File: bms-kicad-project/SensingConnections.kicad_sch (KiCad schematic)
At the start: 29 parts, among them J10 XT60PW-F, J11 1053131302, J12 XT60PW-F, J13 1053131302, J14 1053131303, J15 XT60PW-F, J16 SM06B-GHS-TB, J17 5024940670, J6 XT60PW-F, J7 1053131302, J8 XT60PW-M, J9 1053131302, U8 ACS72981KLRATR-150B5

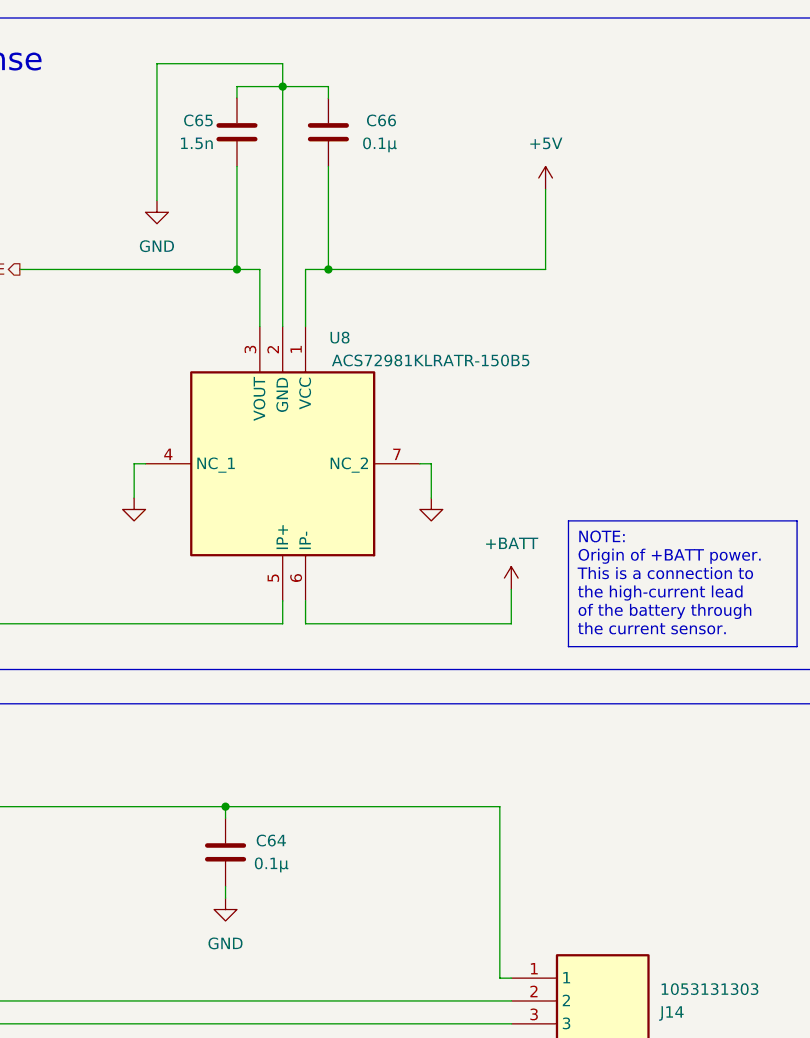
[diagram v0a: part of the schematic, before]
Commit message: feat: added sims directory, new cell balancing components
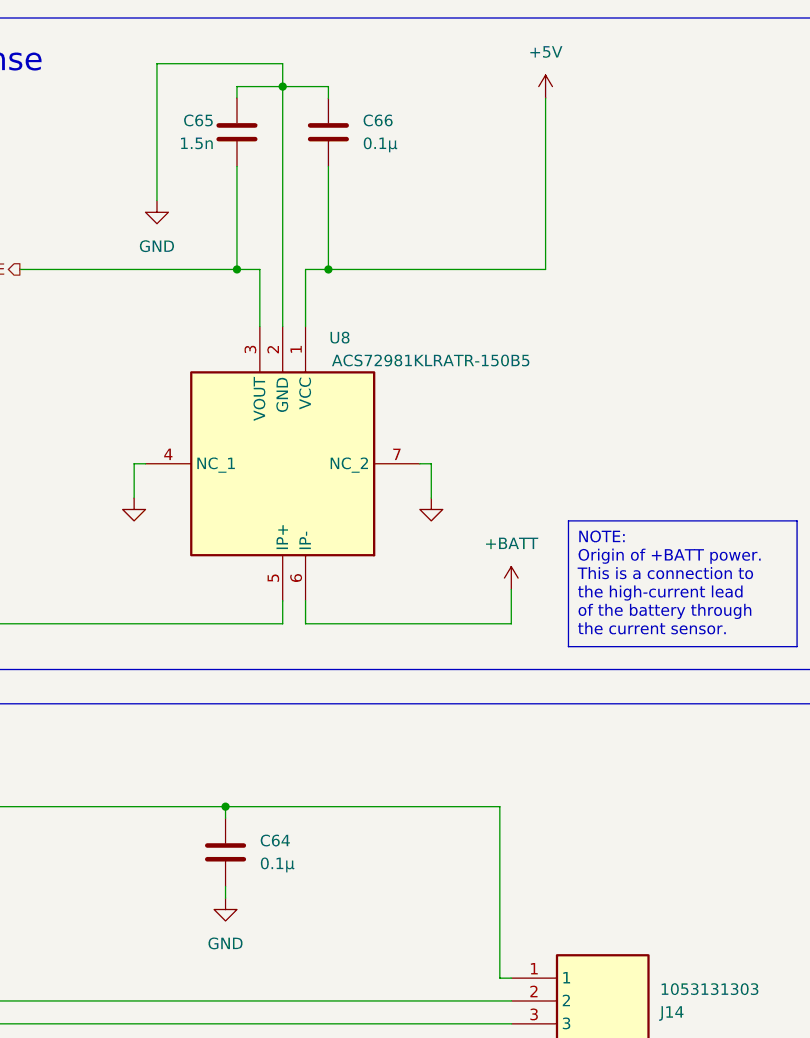
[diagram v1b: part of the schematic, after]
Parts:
- removed C64, C66: 0.1µ, FixedWing:G-21_MUR, symbol FixedWing:GCM21BR72A104KA37L
- added C64, C66: 0.1µ, FixedWing:CAP_GCJ-18_MUR, symbol FixedWing:GCJ188R72A104KA01D
- J10, J12, J15, J6: Manufacturer (none) -> Amass
- J8: Manufacturer (none) -> Changzou Amass Elec
- R109, R110: Manufacturer (none) -> Vishay; Manufacturer Part Number (none) -> CRCW0805100RFKEA
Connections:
- net +5V: now also C64.2, C66.1
- net GND: now also C64.1, C66.2
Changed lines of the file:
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@@
     (stroke (width 0) (type default))
   )
-  (wire (pts (xy 124.46 34.29) (xy 124.46 43.18))
+  (wire (pts (xy 124.46 24.13) (xy 124.46 43.18))
     (stroke (width 0) (type default))
   )
@@
       (effects (font (size 1.27 1.27)) (justify left top) hide)
     )
+    (property "Manufacturer" "Vishay" (at 104.14 884.15 0)
+      (effects (font (size 1.27 1.27)) (justify left top) hide)
+    )
+    (property "Manufacturer Part Number" "CRCW0805100RFKEA" (at 104.14 984.15 0)
+      (effects (font (size 1.27 1.27)) (justify left top) hide)
+    )
     (pin "2")
     (pin "1")
@@
     )
     (property "Arrow Price/Stock" "" (at 26.67 -945.39 0)
+      (effects (font (size 1.27 1.27)) (justify left top) hide)
+    )
+    (property "Manufacturer" "Changzou Amass Elec" (at 26.67 -445.39 0)
       (effects (font (size 1.27 1.27)) (justify left top) hide)
     )
@@
     )
   )
-  (symbol (lib_id "FixedWing:GCM21BR72A104KA37L") (at 100.33 24.13 90) (mirror x) (unit 1)
-    (in_bom yes) (on_board yes) (dnp no)
-    (property "Reference" "C66" (at 107.95 26.67 90)
-      (effects (font (size 1.27 1.27)) (justify left))
-    )
-    (property "Value" "0.1µ" (at 107.95 29.21 90)
-      (effects (font (size 1.27 1.27)) (justify left))
-    )
-    (property "Footprint" "FixedWing:G-21_MUR" (at 86.36 24.13 0)
-      (effects (font (size 1.27 1.27) italic) hide)
-    )
-    (property "Datasheet" "https://search.murata.co.jp/Ceramy/image/img/A01X/G101/ENG/GCJ21BR71A106KE01-01A.pdf" (at 88.9 24.13 0)
-      (effects (font (size 1.27 1.27) italic) hide)
-    )
-    (property "Manufacturer" "Murata Electronics" (at 91.44 24.13 0)
-      (effects (font (size 1.27 1.27)) hide)
-    )
-    (property "Manufacturer Part Number" "GCM21BR72A104KA37L" (at 93.98 24.13 0)
-      (effects (font (size 1.27 1.27)) hide)
-    )
-    (pin "1")
-    (pin "2")
-    (instances
-      (project "bms-board"
-        (path "/8a7831d1-a913-4f04-8780-225d2234b41d/9cf0d325-c2d4-4535-a4db-163de33edbd1"
-          (reference "C66") (unit 1)
-        )
-      )
-    )
-  )
   (symbol (lib_id "FixedWing:XT60PW-F") (at 234.95 46.99 0) (unit 1)
     (in_bom yes) (on_board yes) (dnp no)
@@
     )
     (property "Arrow Price/Stock" "" (at 254 1041.91 0)
+      (effects (font (size 1.27 1.27)) (justify left top) hide)
+    )
+    (property "Manufacturer" "Amass" (at 254 541.91 0)
       (effects (font (size 1.27 1.27)) (justify left top) hide)
     )
@@
     )
   )
+  (symbol (lib_id "FixedWing:GCJ188R72A104KA01D") (at 88.9 111.76 90) (unit 1)
+    (in_bom yes) (on_board yes) (dnp no) (fields_autoplaced)
+    (property "Reference" "C64" (at 92.71 106.68 90)
+      (effects (font (size 1.27 1.27)) (justify right))
+    )
+    (property "Value" "0.1µ" (at 92.71 109.22 90)
+      (effects (font (size 1.27 1.27)) (justify right))
+    )
+    (property "Footprint" "FixedWing:CAP_GCJ-18_MUR" (at 77.47 114.3 0)
+      (effects (font (size 1.27 1.27) italic) hide)
+    )
+    (property "Datasheet" "https://search.murata.co.jp/Ceramy/image/img/A01X/G101/ENG/GCJ21BR71A106KE01-01A.pdf" (at 77.47 114.3 0)
+      (effects (font (size 1.27 1.27) italic) hide)
+    )
+    (property "Manufacturer" "Murata Electronics" (at 77.47 113.03 0)
+      (effects (font (size 1.27 1.27)) hide)
+    )
+    (property "Manufacturer Part Number" "GCJ188R72A104KA01D" (at 77.47 114.3 0)
+      (effects (font (size 1.27 1.27)) hide)
+    )
+    (pin "2")
+    (pin "1")
+    (instances
+      (project "bms-board"
+        (path "/8a7831d1-a913-4f04-8780-225d2234b41d/9cf0d325-c2d4-4535-a4db-163de33edbd1"
+          (reference "C64") (unit 1)
+        )
+      )
+    )
+  )
   (symbol (lib_id "Mechanical:MountingHole_Pad") (at 406.4 217.17 90) (mirror x) (unit 1)
     (in_bom yes) (on_board yes) (dnp no) (fields_autoplaced)
@@
     )
     (property "Arrow Price/Stock" "" (at 288.29 1041.91 0)
+      (effects (font (size 1.27 1.27)) (justify left top) hide)
+    )
+    (property "Manufacturer" "Amass" (at 288.29 541.91 0)
       (effects (font (size 1.27 1.27)) (justify left top) hide)
     )
@@
     )
   )
-  (symbol (lib_id "power:+5V") (at 124.46 34.29 0) (unit 1)
-    (in_bom yes) (on_board yes) (dnp no) (fields_autoplaced)
-    (property "Reference" "#PWR067" (at 124.46 38.1 0)
-      (effects (font (size 1.27 1.27)) hide)
-    )
-    (property "Value" "+5V" (at 124.46 29.21 0)
-      (effects (font (size 1.27 1.27)))
-    )
-    (property "Footprint" "" (at 124.46 34.29 0)
-      (effects (font (size 1.27 1.27)) hide)
-    )
-    (property "Datasheet" "" (at 124.46 34.29 0)
+  (symbol (lib_id "power:+5V") (at 124.46 24.13 0) (unit 1)
+    (in_bom yes) (on_board yes) (dnp no) (fields_autoplaced)
+    (property "Reference" "#PWR067" (at 124.46 27.94 0)
+      (effects (font (size 1.27 1.27)) hide)
+    )
+    (property "Value" "+5V" (at 124.46 19.05 0)
+      (effects (font (size 1.27 1.27)))
+    )
+    (property "Footprint" "" (at 124.46 24.13 0)
+      (effects (font (size 1.27 1.27)) hide)
+    )
+    (property "Datasheet" "" (at 124.46 24.13 0)
       (effects (font (size 1.27 1.27)) hide)
     )
@@
     )
   )
-  (symbol (lib_id "FixedWing:GCM21BR72A104KA37L") (at 88.9 111.76 90) (unit 1)
-    (in_bom yes) (on_board yes) (dnp no)
-    (property "Reference" "C64" (at 93.98 106.68 90)
-      (effects (font (size 1.27 1.27)))
-    )
-    (property "Value" "0.1µ" (at 93.98 109.22 90)
-      (effects (font (size 1.27 1.27)))
-    )
-    (property "Footprint" "FixedWing:G-21_MUR" (at 74.93 111.76 0)
-      (effects (font (size 1.27 1.27) italic) hide)
-    )
-    (property "Datasheet" "https://search.murata.co.jp/Ceramy/image/img/A01X/G101/ENG/GCJ21BR71A106KE01-01A.pdf" (at 77.47 111.76 0)
-      (effects (font (size 1.27 1.27) italic) hide)
-    )
-    (property "Manufacturer" "Murata Electronics" (at 80.01 111.76 0)
-      (effects (font (size 1.27 1.27)) hide)
-    )
-    (property "Manufacturer Part Number" "GCM21BR72A104KA37L" (at 82.55 111.76 0)
-      (effects (font (size 1.27 1.27)) hide)
-    )
-    (pin "1")
-    (pin "2")
-    (instances
-      (project "bms-board"
-        (path "/8a7831d1-a913-4f04-8780-225d2234b41d/9cf0d325-c2d4-4535-a4db-163de33edbd1"
-          (reference "C64") (unit 1)
-        )
-      )
-    )
-  )
   (symbol (lib_id "FixedWing:XT60PW-F") (at 200.66 46.99 0) (unit 1)
     (in_bom yes) (on_board yes) (dnp no)
@@
     )
     (property "Arrow Price/Stock" "" (at 219.71 1041.91 0)
+      (effects (font (size 1.27 1.27)) (justify left top) hide)
+    )
+    (property "Manufacturer" "Amass" (at 219.71 541.91 0)
       (effects (font (size 1.27 1.27)) (justify left top) hide)
     )
@@
       (effects (font (size 1.27 1.27)) (justify left top) hide)
     )
+    (property "Manufacturer" "Vishay" (at 113.03 884.15 0)
+      (effects (font (size 1.27 1.27)) (justify left top) hide)
+    )
+    (property "Manufacturer Part Number" "CRCW0805100RFKEA" (at 113.03 984.15 0)
+      (effects (font (size 1.27 1.27)) (justify left top) hide)
+    )
     (pin "1")
     (pin "2")
@@
     )
   )
+  (symbol (lib_id "FixedWing:GCJ188R72A104KA01D") (at 100.33 31.75 90) (unit 1)
+    (in_bom yes) (on_board yes) (dnp no) (fields_autoplaced)
+    (property "Reference" "C66" (at 104.14 26.67 90)
+      (effects (font (size 1.27 1.27)) (justify right))
+    )
+    (property "Value" "0.1µ" (at 104.14 29.21 90)
+      (effects (font (size 1.27 1.27)) (justify right))
+    )
+    (property "Footprint" "FixedWing:CAP_GCJ-18_MUR" (at 88.9 34.29 0)
+      (effects (font (size 1.27 1.27) italic) hide)
+    )
+    (property "Datasheet" "https://search.murata.co.jp/Ceramy/image/img/A01X/G101/ENG/GCJ21BR71A106KE01-01A.pdf" (at 88.9 34.29 0)
+      (effects (font (size 1.27 1.27) italic) hide)
+    )
+    (property "Manufacturer" "Murata Electronics" (at 88.9 33.02 0)
+      (effects (font (size 1.27 1.27)) hide)
+    )
+    (property "Manufacturer Part Number" "GCJ188R72A104KA01D" (at 88.9 34.29 0)
+      (effects (font (size 1.27 1.27)) hide)
+    )
+    (pin "1")
+    (pin "2")
+    (instances
+      (project "bms-board"
+        (path "/8a7831d1-a913-4f04-8780-225d2234b41d/9cf0d325-c2d4-4535-a4db-163de33edbd1"
+          (reference "C66") (unit 1)
+        )
+      )
+    )
+  )
   (symbol (lib_id "power:+BATT") (at 165.1 30.48 0) (unit 1)
     (in_bom yes) (on_board yes) (dnp no) (fields_autoplaced)
@@
       (effects (font (size 1.27 1.27)) (justify left top) hide)
     )
+    (property "Manufacturer" "Amass" (at 185.42 541.91 0)
+      (effects (font (size 1.27 1.27)) (justify left top) hide)
+    )

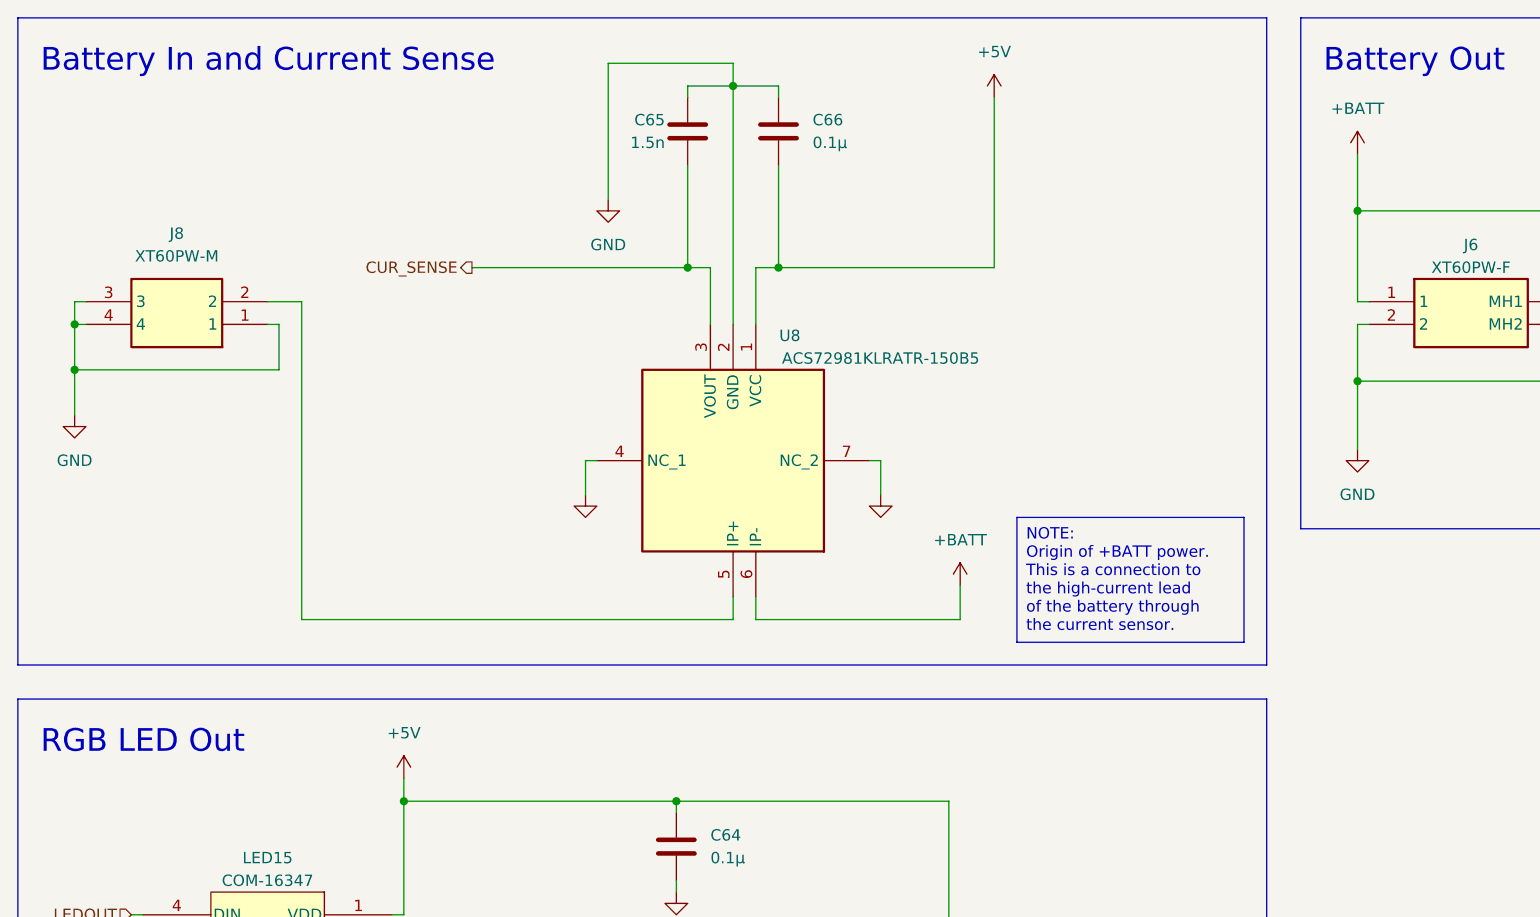
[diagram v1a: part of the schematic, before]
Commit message: feat: cell filtering/balancing switchover done
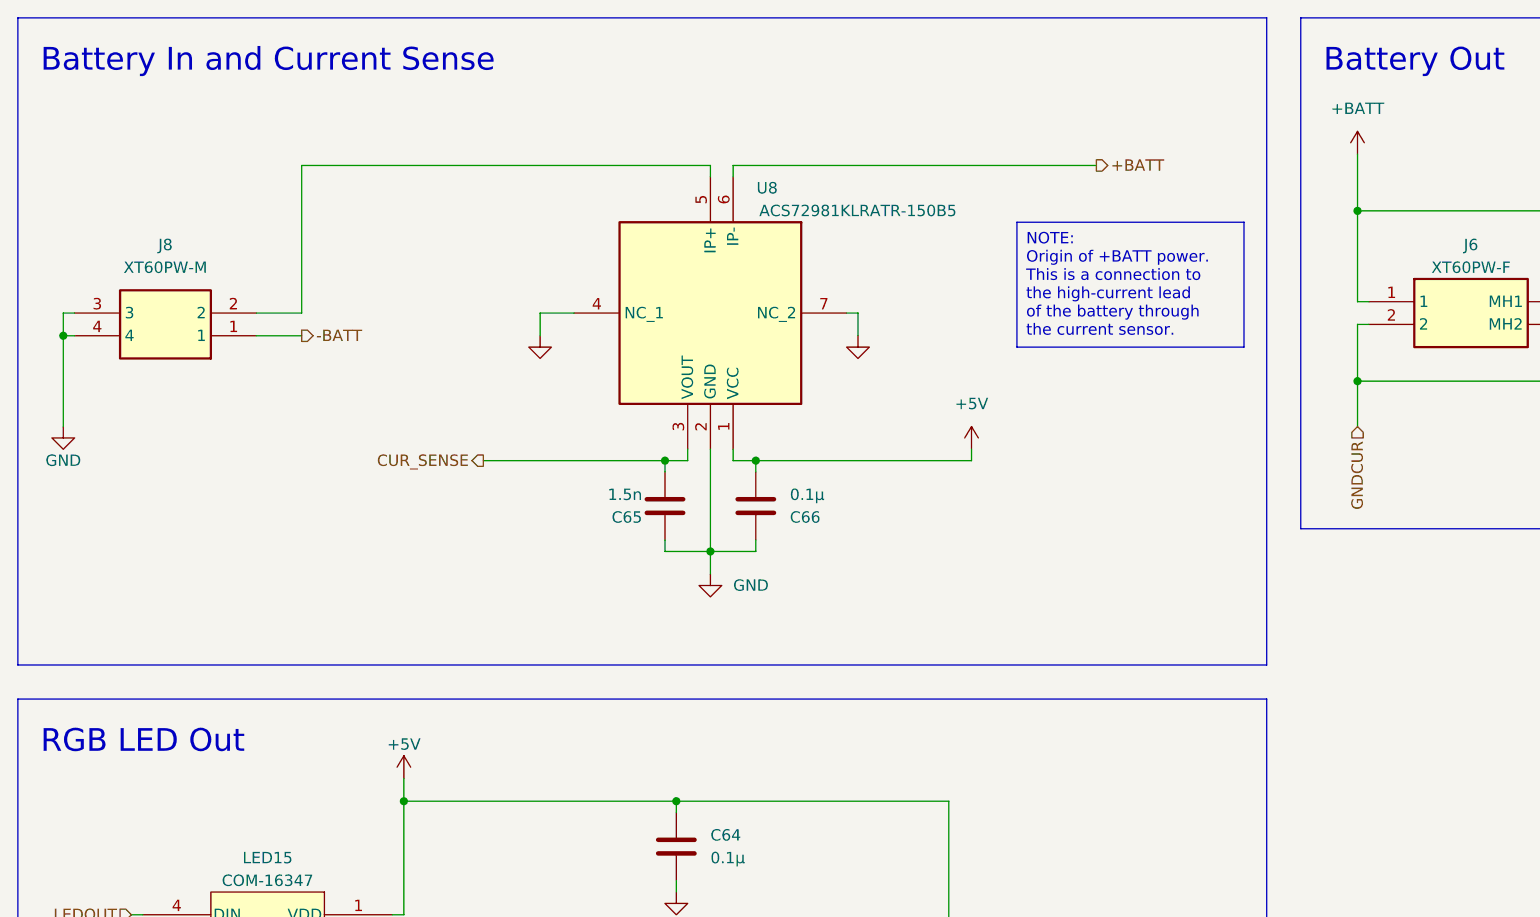
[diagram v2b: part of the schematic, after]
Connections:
- net GND: no longer J10.2, J10.3 (MH1), J10.4 (MH2), J12.2, J12.3 (MH1), J12.4 (MH2), J15.2, J15.3 (MH1), J15.4 (MH2), J6.2, J6.3 (MH1), J6.4 (MH2), J8.1
- new net -BATT: J8.1
- new net GNDCUR: J10.2, J10.3 (MH1), J10.4 (MH2), J12.2, J12.3 (MH1), J12.4 (MH2), J15.2, J15.3 (MH1), J15.4 (MH2), J6.2, J6.3 (MH1), J6.4 (MH2)
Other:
- moved on the sheet: C65, C66, J8, U8

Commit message: feat: don't even know what I changed, just zoned out for several hours. Made PCB r/a mount XT-60s and solder pads into a 2-for-1 deal
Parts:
- added J18: XT60PW-F, FixedWing:XT60PWF, symbol FixedWing:XT60PW-F
- J13: renamed from J15; footprint FixedWing:XT60PWF -> FixedWing:XT60PWF_Pad
- J6: renamed from J8; footprint FixedWing:XT60PWM -> FixedWing:XT60PWM_Pad
- renumbered C64 to C66, C66 to C67, J6 to J10, J10 to J11, J7 to J14, J9 to J15, J11 to J16, J13 to J17, J17 to J7, J14 to J8, J16 to J9, R108 to R120, R109 to R121, R110 to R122, R111 to R123, U8 to U7
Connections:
- net +BATT: now also J18.1
- net GND: now also J10.3 (MH1), J10.4 (MH2), J11.3 (MH1), J11.4 (MH2), J12.3 (MH1), J12.4 (MH2), J9.7, J9.8, J18.3 (MH1), J18.4 (MH2); no longer J6.3, J6.4
- net GNDCUR: now also J18.2; no longer J10.3 (MH1), J10.4 (MH2), J11.3 (MH1), J11.4 (MH2), J12.3 (MH1), J12.4 (MH2), J13.3 (MH1), J13.4 (MH2)
- net RGB_DOUT: now reaches J8.2, LED15.2 (DOUT)
- net LEDOUT renamed RGB_DIN
- no-connect marks 0 -> 4
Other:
- moved on the sheet: C66, J11, J12, J13, J14, J15, J16, J17, J7, J8, LED15, R120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

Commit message: feat: schematic pretty much done
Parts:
- added TP19, TP20, TP21: TestPoint, TestPoint:TestPoint_Pad_D1.5mm, symbol Connector:TestPoint
- renumbered C66 to C65, C65 to C66, J12 to J10, J18 to J11, J8 to J12, J9 to J13, J13 to J14, J14 to J15, J15 to J16, J16 to J17, J17 to J18, J10 to J6, J6 to J7, J11 to J8, J7 to J9
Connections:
- net +BATT: now also TP21.1
- net CUR_SENSE: now also TP19.1
- net GND: no longer J15.2, J16.2, J17.2, J18.2
- net GNDCUR: now also J15.2, J16.2, J17.2, J18.2
- net at J7.2, U7.5 (IP+): now also TP20.1
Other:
- moved on the sheet: C66, C67, H1, H2, H3, H4, H5, H6, H7, H8, J10, J11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
